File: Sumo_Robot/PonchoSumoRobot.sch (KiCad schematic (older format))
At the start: 34 parts, among them K1 RELAY_C, K2 RELAY_C, K3 RELAY_C, K4 RELAY_C, P1 CONN_01X02, P2 CONN_01X04, P3 CONN_02X09, P4 CONN_01X02, P5 CONN_01X02, P6 CONN_01X04, P7 CONN_01X02, P8 CONN_01X02, Q1 2SC1945, Q2 2SC1945, Q3 2SC1945, Q4 2SC1945, Q5 2SC1945

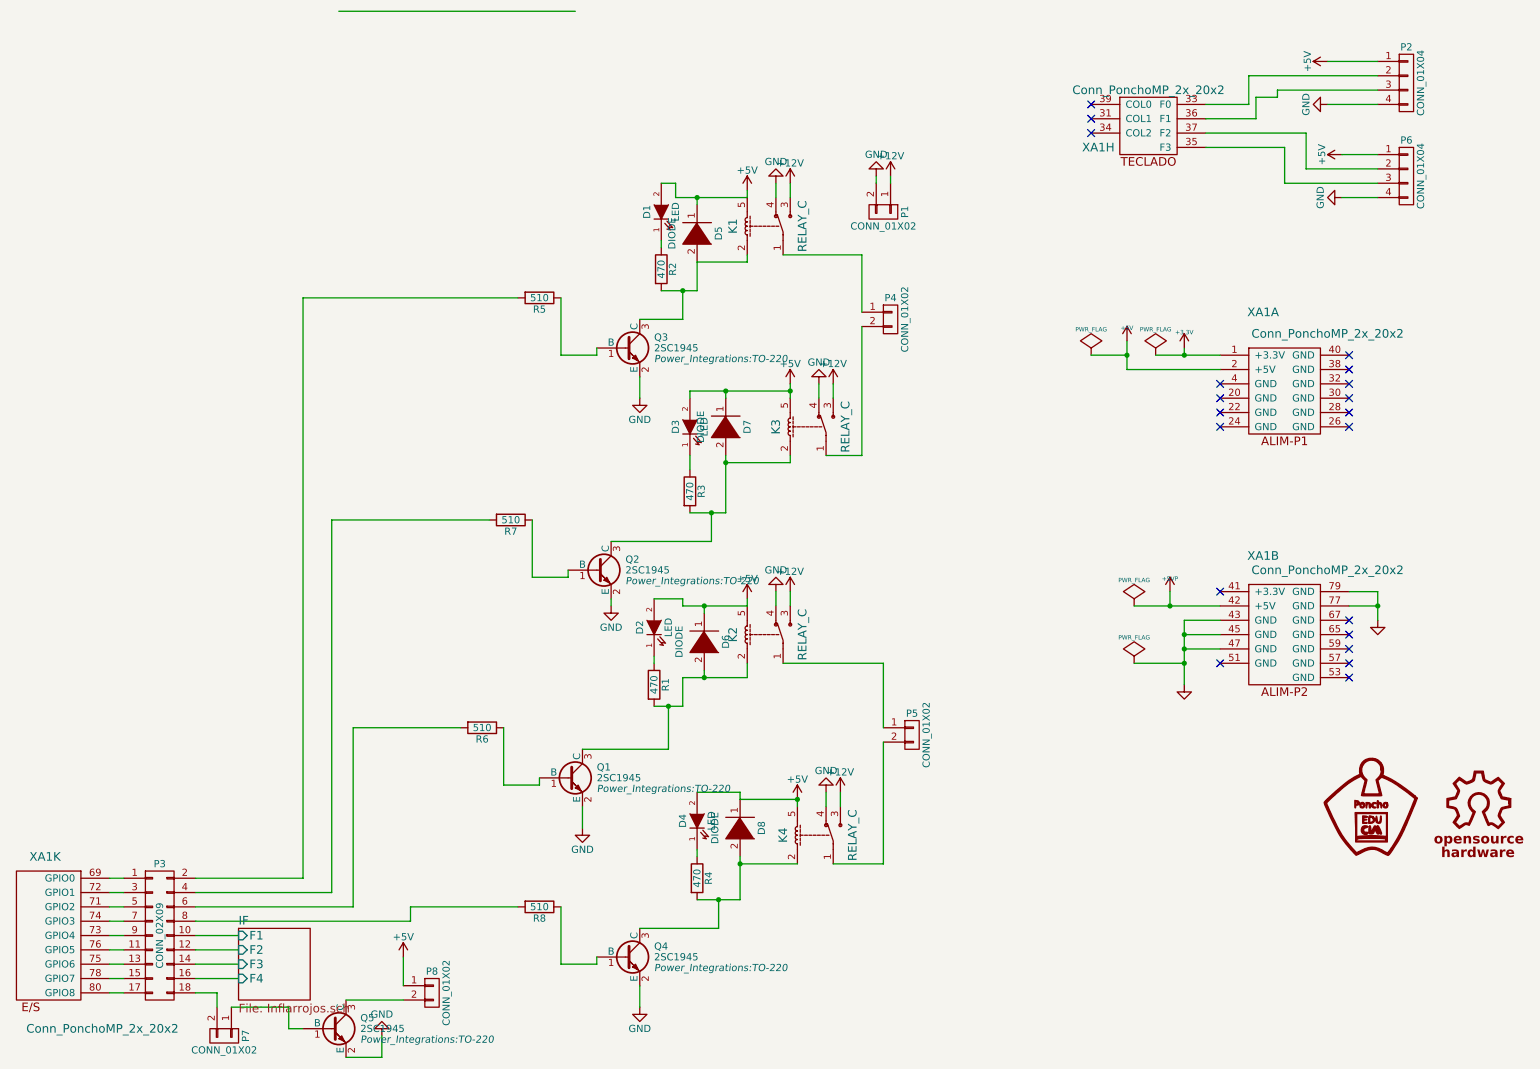
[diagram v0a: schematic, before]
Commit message: Poncho Sumo Robot: Emprolijo esquemático, serigrafías, vista 3D y textos.
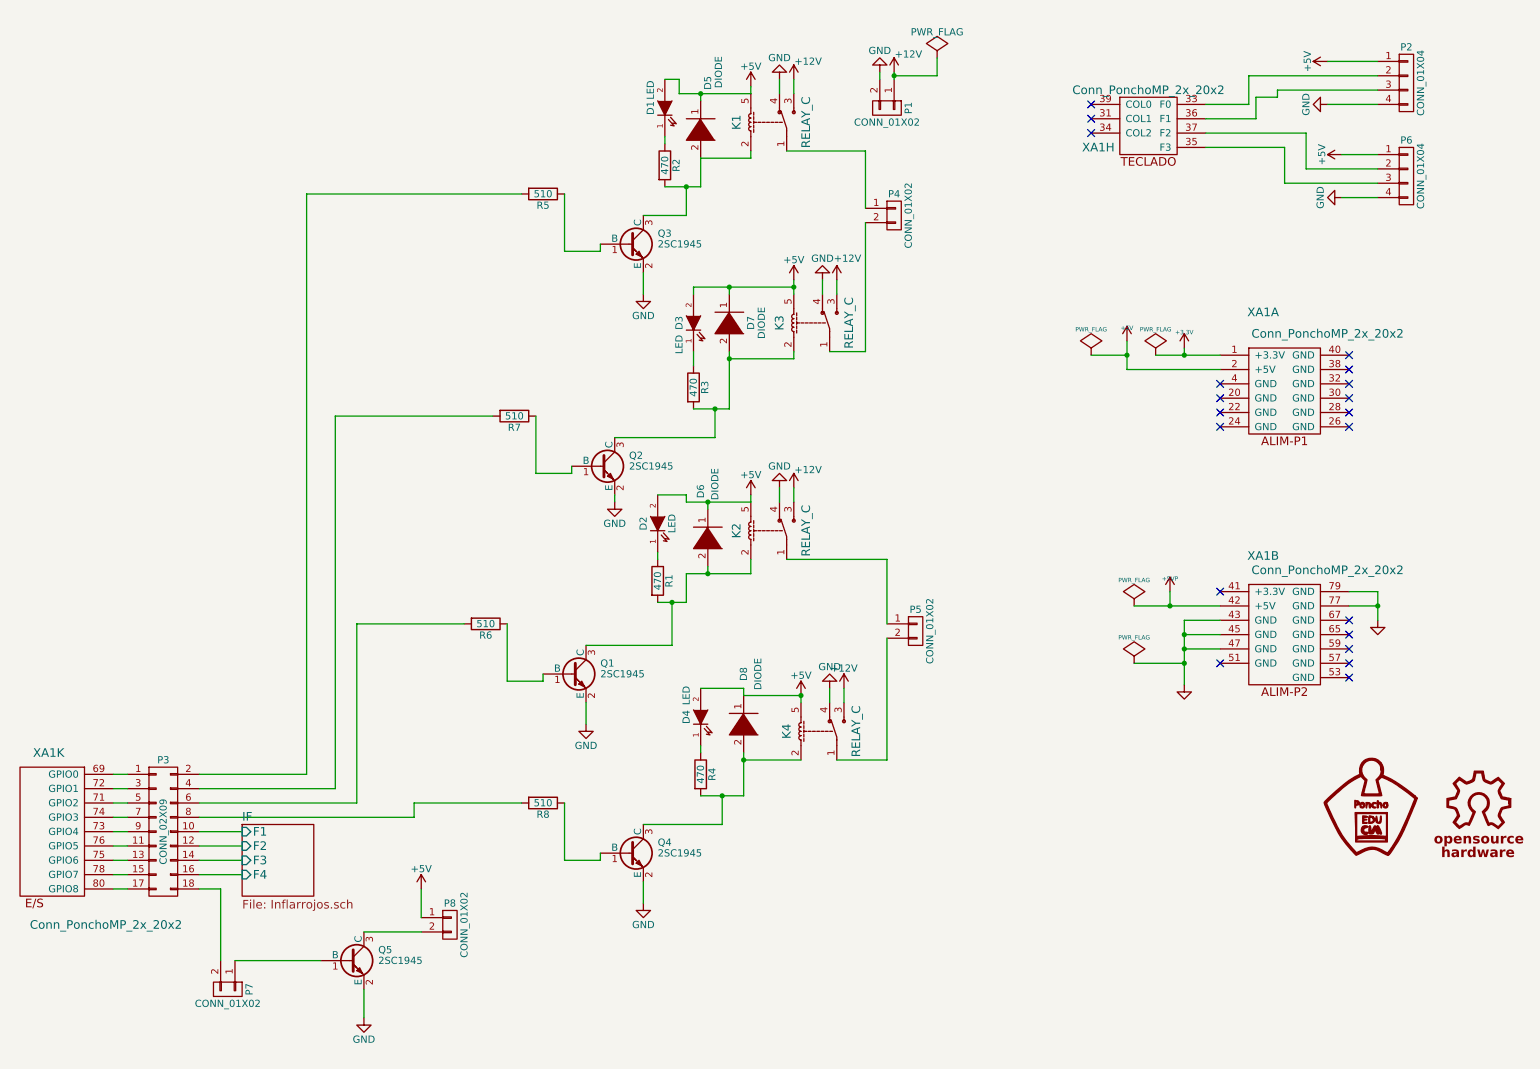
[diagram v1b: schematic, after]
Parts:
- R1, R2, R3, R4, R5, R6, R7, R8: footprint sumo_robot:Resistor_Horizontal_RM7mm -> sumo_robot:Resistor_Horizontal_RM7m
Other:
- moved on the sheet: D1, D2, D3, D4, D5, D6, D7, D8, K1, K2, K3, K4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
